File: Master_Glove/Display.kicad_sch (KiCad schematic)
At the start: 0 parts

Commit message: Conversion + Display Schematic. Missing forced ground on ADC booth
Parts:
- added C10, C11, C12, C13, C14, C15, C16, C8, C9: 150pF, symbol Device:C_Small
- added LED1, LED2, LED3: SM410501N/8, Library:LED-SEG-TH_10P-L12.7-W19.0-P2.54-S15.24-BL, symbol Library:SM410501N_8
- added R10, R15, R16, R17, R18, R19, R20, R21, R22, R23, R24, R25, R26, R27, R28, R29, R30, R31, R32, R33, R34: R_US, symbol Device:R_US
- added R35, R36: 10k, symbol Device:R_US
- added RV1: R_Potentiometer_US, symbol Device:R_Potentiometer_US
- added U10, U8, U9: CD4543BM96, Library:SOIC-16_L9.9-W3.9-P1.27-LS6.0-BL, symbol Library:CD4543BM96
- added U11: BCD_CONVERTER, symbol Library:8BIT_BCD_CONVERTER
- added U12: ADC0804LCWM/NOPB, symbol Library:ADC0804LCWM_NOPB
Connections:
- new net: R28.1, U10.14 (g)
- new net: LED3.10 (g), R28.2
- new net: R20.1, U8.14 (g)
- new net: LED1.10 (g), R20.2
- new net: R27.1, U9.9 (a)
- new net: LED2.7 (a), R27.2
- new net: R26.1, U9.10 (b)
- new net: R25.1, U9.11 (c)
- new net: R24.1, U9.12 (d)
- new net: R23.1, U9.13 (e)
- new net: R21.1, U9.14 (g)
- new net: R22.1, U9.15 (f)
- new net: LED2.4 (c), R25.2
- new net: LED2.1 (e), R23.2
- new net: LED2.10 (g), R21.2
- new net: LED2.2 (d), R24.2
- new net: LED2.6 (b), R26.2
- new net: LED2.9 (f), R22.2
- new net: R19.1, U8.15 (f)
- new net: LED1.9 (f), R19.2
- new net: LED3.1 (e), R30.2
- new net: LED3.2 (d), R31.2
- new net: LED3.4 (c), R32.2
- new net: LED3.6 (b), R33.2
- new net: LED3.7 (a), R34.2
- new net: LED3.9 (f), R29.2
- new net: R10.1, U8.9 (a)
- new net: LED1.7 (a), R10.2
- new net: R31.1, U10.12 (d)
- new net: U11. (O0), U12.11 (DB7)
- new net: U11. (O0), U12.12 (DB6)
- new net: U11. (O0), U12.13 (DB5)
- new net: U11. (O0), U12.14 (DB4)
- new net: U11. (O0), U12.15 (DB3)
- new net: U11. (O0), U12.16 (DB2)
- new net: U11. (O0), U12.17 (DB1)
- new net: U11. (O0), U12.18 (DB0)
- new net: R15.1, U8.10 (b)
- new net: R16.1, U8.11 (c)
- new net: R17.1, U8.12 (d)
- new net: R18.1, U8.13 (e)
- new net: LED1.1 (e), R18.2
- new net: LED1.2 (d), R17.2
- new net: R29.1, U10.15 (f)
- new net: LED1.4 (c), R16.2
- new net: R33.1, U10.10 (b)
- new net: R32.1, U10.11 (c)
- new net: R30.1, U10.13 (e)
- new net: R34.1, U10.9 (a)
- new net: U12.3 (WR), U12.5 (INTR)
- new net: LED1.6 (b), R15.2
- new net CLKIN: C8.1, R35.2, U12.4 (CLKIN)
- new net CLKR: R35.1, U12.19 (CLKR)
- new net GND: C10.1, C11.1, C12.1, C13.1, C14.1, C15.1, C16.1, C8.2, C9.1, RV1.2, U10.7 (BLNK), U10.8 (VSS), U11. (O0), U12.1 (CS), U12.10 (DGND), U12.2 (RD), U12.7 (VIN(–)), U12.8 (AGND), U8.2 (C), U8.4 (D), U8.7 (BLNK), U8.8 (VSS), U9.7 (BLNK), U9.8 (VSS)
- new net Hunds0: U11. (O0), U8.5 (A)
- new net Hunds1: U11. (O0), U8.3 (B)
- new net LATCH: U10.1 (LD), U8.1 (LD), U9.1 (LD)
- new net Ones0: U10.5 (A), U11. (O0)
- new net Ones1: U10.3 (B), U11. (O0)
- new net Ones2: U10.2 (C), U11. (O0)
- new net Ones3: U10.4 (D), U11. (O0)
- new net Tens0: U11. (O0), U9.5 (A)
- new net Tens1: U11. (O0), U9.3 (B)
- new net Tens2: U11. (O0), U9.2 (C)
- new net Tens3: U11. (O0), U9.4 (D)
- new net VCC: C10.2, C11.2, C12.2, C13.2, C14.2, C15.2, C16.2, C9.2, LED1.3 (G1), LED1.8 (G1), LED2.3 (G1), LED2.8 (G1), LED3.3 (G1), LED3.8 (G1), R36.2, U10.16 (VDD), U10.6 (PH), U11. (O0), U12.20 (VCC), U8.16 (VDD), U8.6 (PH), U9.16 (VDD), U9.6 (PH)
- new net VREF/2: R36.1, RV1.1, U12.9 (VREF/2)
- new net V_MATH: U12.6 (VIN(+))
- no-connect marks 0 -> 4

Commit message: Power
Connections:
- net ADC_INIT: now reaches U12.3 (WR), U12.5 (INTR)
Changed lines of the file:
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@@
 	(wire
 		(pts
-			(xy 116.84 76.2) (xy 119.38 76.2)
+			(xy 115.57 76.2) (xy 119.38 76.2)
 		)
 		(stroke
@@
 	(global_label "CLKIN"
 		(shape input)
-		(at 116.84 76.2 180)
-		(fields_autoplaced yes)
-		(effects
-			(font
-				(size 1.27 1.27)
-			)
-			(justify right)
-		)
-		(property "Intersheetrefs" "${INTERSHEET_REFS}"
-			(at 108.3514 76.2 0)
+		(at 115.57 76.2 180)
+		(fields_autoplaced yes)
+		(effects
+			(font
+				(size 1.27 1.27)
+			)
+			(justify right)
+		)
+		(property "Intersheetrefs" "${INTERSHEET_REFS}"
+			(at 107.0814 76.2 0)
 			(effects
 				(font
@@
 				(hide yes)
 			)
+		)
+	)
+	(global_label "ADC_INIT"
+		(shape input)
+		(at 118.11 78.74 180)
+		(fields_autoplaced yes)
+		(effects
+			(font
+				(size 1.27 1.27)
+			)
+			(justify right)
+		)
+		(property "Intersheetrefs" "${INTERSHEET_REFS}"
+			(at 107.0209 78.74 0)
+			(effects
+				(font
+					(size 1.27 1.27)
+				)
+				(justify right)
+				(hide yes)
+			)

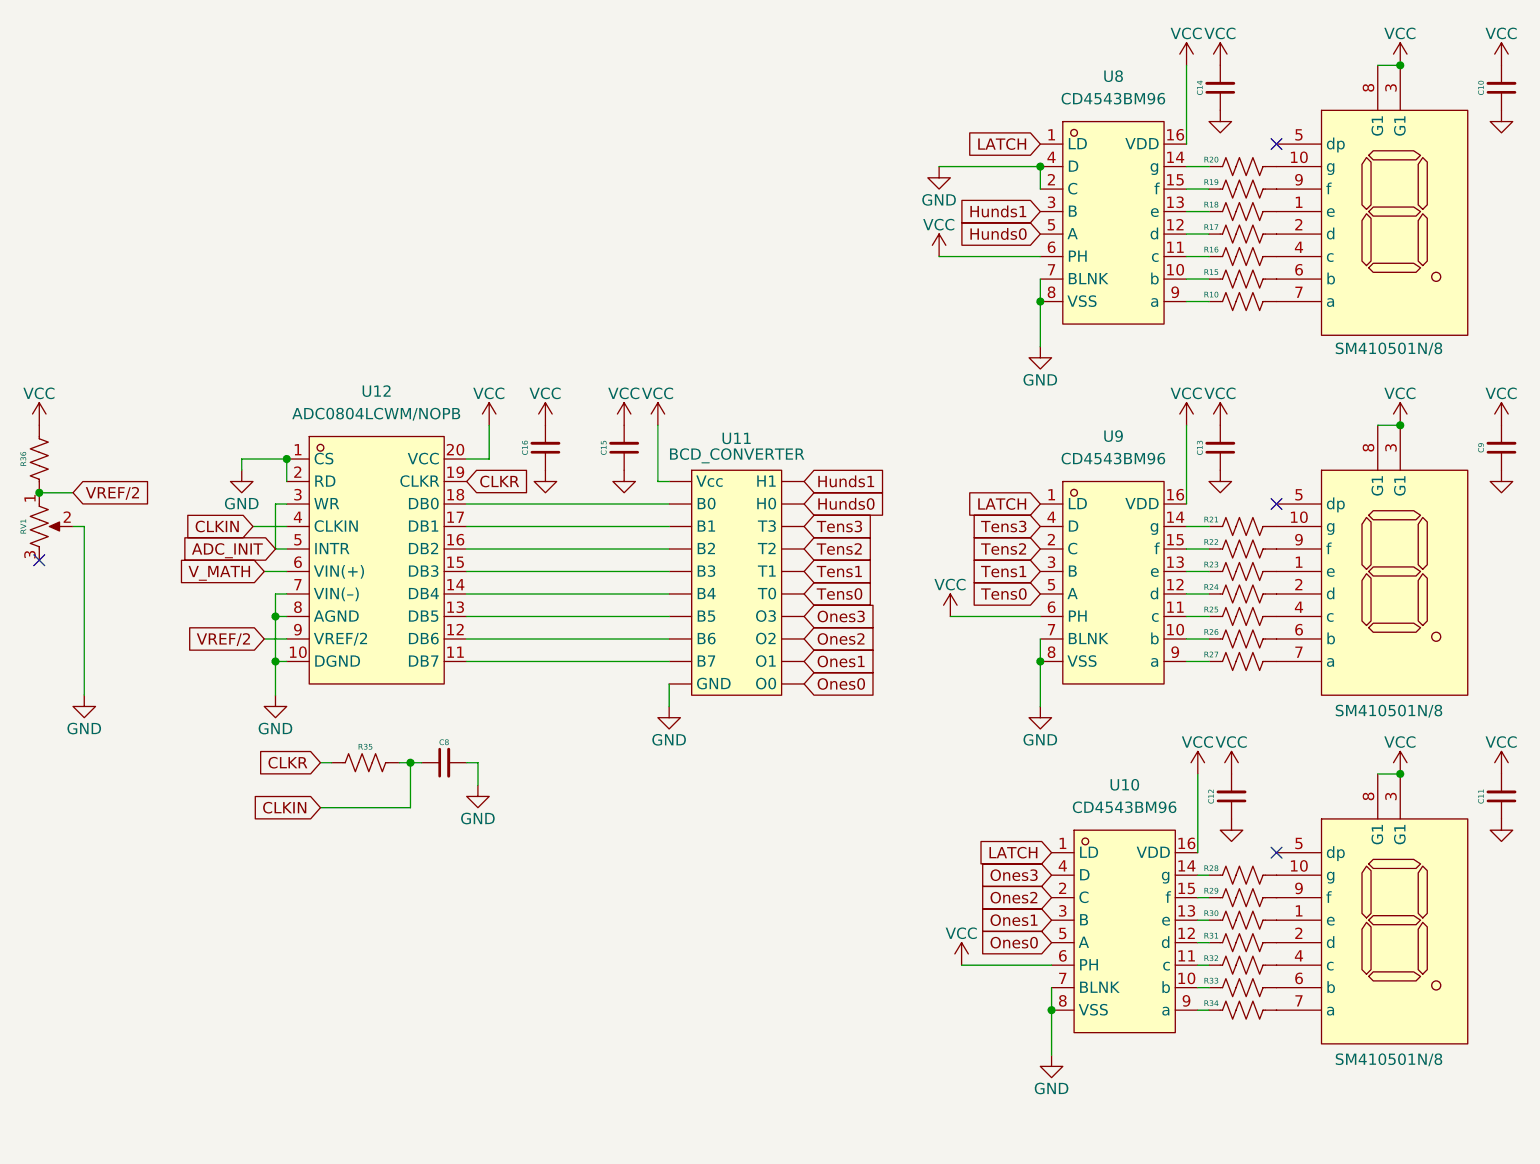
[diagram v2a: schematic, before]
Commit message: Modifications according to reccomendation
Changed Vcc to +5V
Subbed MIC1551 to MIC 1553
Added debounce on button
Fixed other small bugs
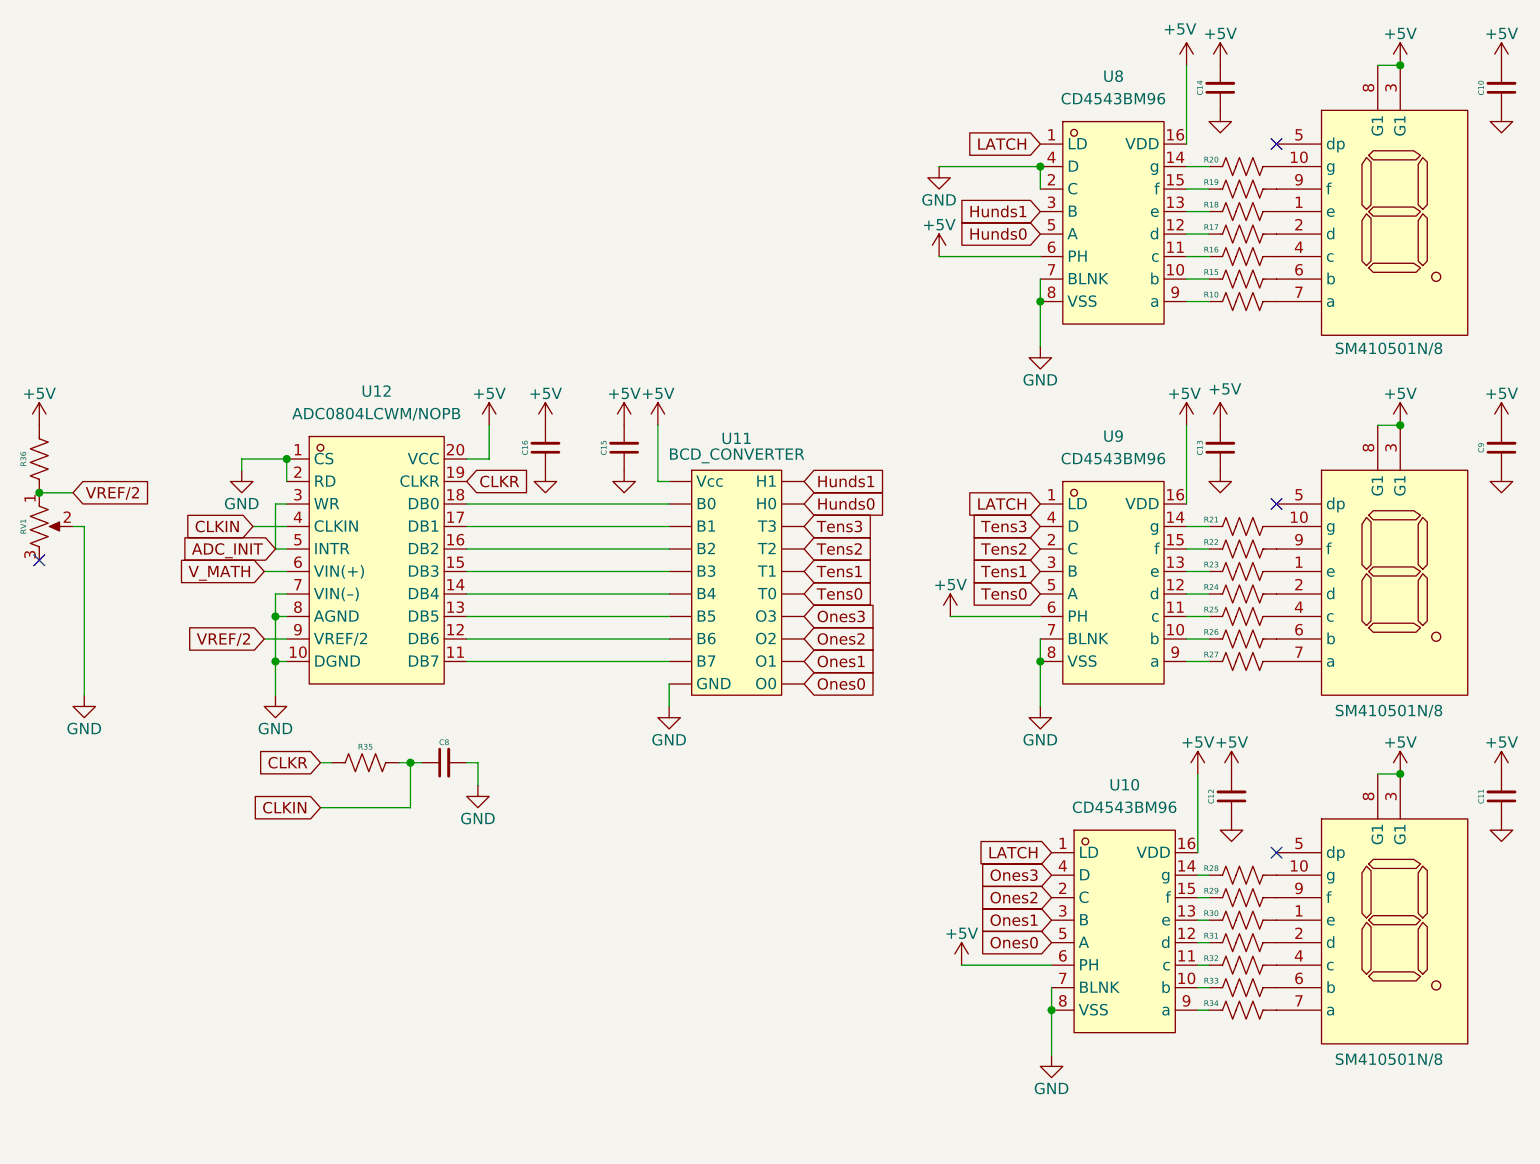
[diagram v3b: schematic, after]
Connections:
- net VCC renamed +5V
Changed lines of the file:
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@@
 			)
 		)
-		(property "Value" "VCC"
+		(property "Value" "+5V"
 			(at 245.11 20.574 0)
 			(effects
@@
 			)
 		)
-		(property "Value" "VCC"
+		(property "Value" "+5V"
 			(at 142.24 61.214 0)
 			(effects
@@
 			)
 		)
-		(property "Value" "VCC"
-			(at 220.98 20.574 0)
+		(property "Value" "+5V"
+			(at 220.218 20.066 0)
 			(effects
 				(font
@@
 			)
 		)
-		(property "Value" "VCC"
+		(property "Value" "+5V"
 			(at 224.79 20.574 0)
 			(effects
@@
 			)
 		)
-		(property "Value" "VCC"
+		(property "Value" "+5V"
 			(at 161.29 61.214 0)
 			(effects
@@
 			)
 		)
-		(property "Value" "VCC"
+		(property "Value" "+5V"
 			(at 256.54 61.214 0)
 			(effects
@@
 			)
 		)
-		(property "Value" "VCC"
+		(property "Value" "+5V"
 			(at 194.31 82.804 0)
 			(effects
@@
 			)
 		)
-		(property "Value" "VCC"
+		(property "Value" "+5V"
 			(at 91.44 61.214 0)
 			(effects
@@
 			)
 		)
-		(property "Value" "VCC"
+		(property "Value" "+5V"
 			(at 226.06 100.584 0)
 			(effects
@@
 			)
 		)
-		(property "Value" "VCC"
+		(property "Value" "+5V"
 			(at 157.48 61.214 0)
 			(effects
@@
 			)
 		)
-		(property "Value" "VCC"
+		(property "Value" "+5V"
 			(at 148.59 61.214 0)
 			(effects
@@
 			)
 		)
-		(property "Value" "VCC"
+		(property "Value" "+5V"
 			(at 256.54 20.574 0)
 			(effects
@@
 			)
 		)
-		(property "Value" "VCC"
+		(property "Value" "+5V"
 			(at 245.11 100.584 0)
 			(effects
@@
 			)
 		)
-		(property "Value" "VCC"
-			(at 220.98 61.214 0)
+		(property "Value" "+5V"
+			(at 220.726 61.214 0)
 			(effects
 				(font
@@
 			)
 		)
-		(property "Value" "VCC"
+		(property "Value" "+5V"
 			(at 195.58 122.174 0)
 			(effects
@@
 			)
 		)
-		(property "Value" "VCC"
-			(at 224.79 61.214 0)
+		(property "Value" "+5V"
+			(at 225.298 60.706 0)
 			(effects
 				(font
@@
 			)
 		)
-		(property "Value" "VCC"
+		(property "Value" "+5V"
 			(at 256.54 100.584 0)
 			(effects
@@
 			)
 		)
-		(property "Value" "VCC"
+		(property "Value" "+5V"
 			(at 193.04 42.164 0)
 			(effects
@@
 			)
 		)
-		(property "Value" "VCC"
+		(property "Value" "+5V"
 			(at 222.25 100.584 0)
 			(effects
@@
 			)
 		)
-		(property "Value" "VCC"
+		(property "Value" "+5V"
 			(at 245.11 61.214 0)
 			(effects

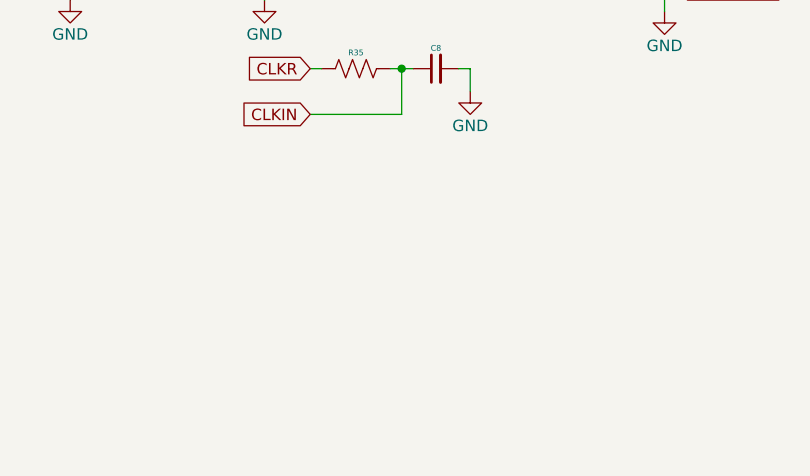
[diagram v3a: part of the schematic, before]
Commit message: ADC init circuit draft
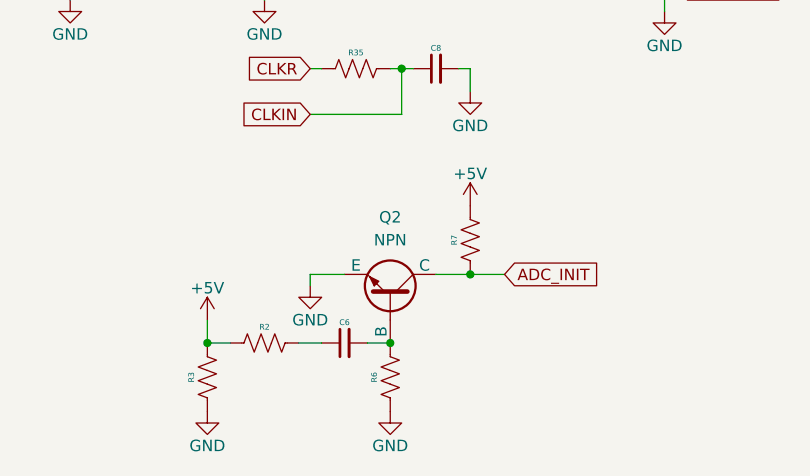
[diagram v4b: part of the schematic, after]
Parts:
- added C6: 150pF, symbol Device:C_Small
- added Q2: NPN, symbol Simulation_SPICE:NPN
- added R2, R3, R6, R7: 10k, symbol Device:R_US
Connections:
- net +5V: now also R2.1, R3.2, R7.2
- net ADC_INIT: now also Q2.1 (C), R7.1
- net GND: now also Q2.3 (E), R3.1, R6.1
- new net: C6.1, R2.2
- new net: C6.2, Q2.2 (B), R6.2
